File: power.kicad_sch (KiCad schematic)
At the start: 31 parts, among them Q4 CSD17575Q3, Q5 CSD17312Q5, U10 DS4432U+, U16 LM27402, U9 INA260

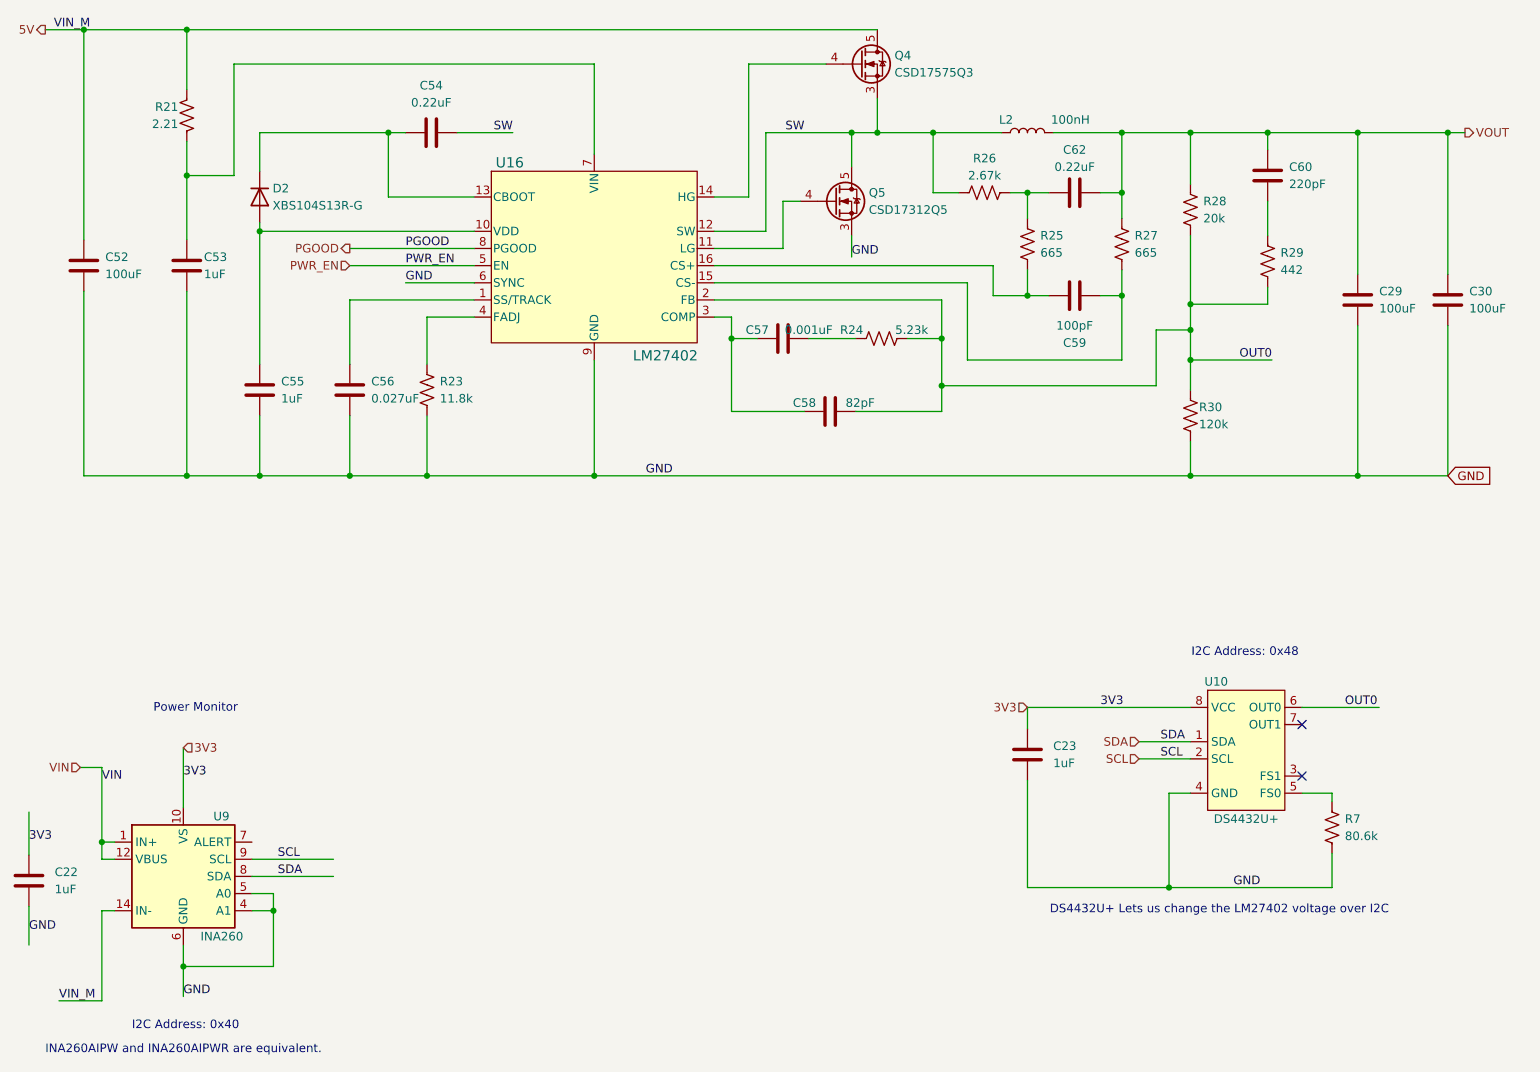
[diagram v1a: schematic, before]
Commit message: changed buttons for #5 flipped display for #2
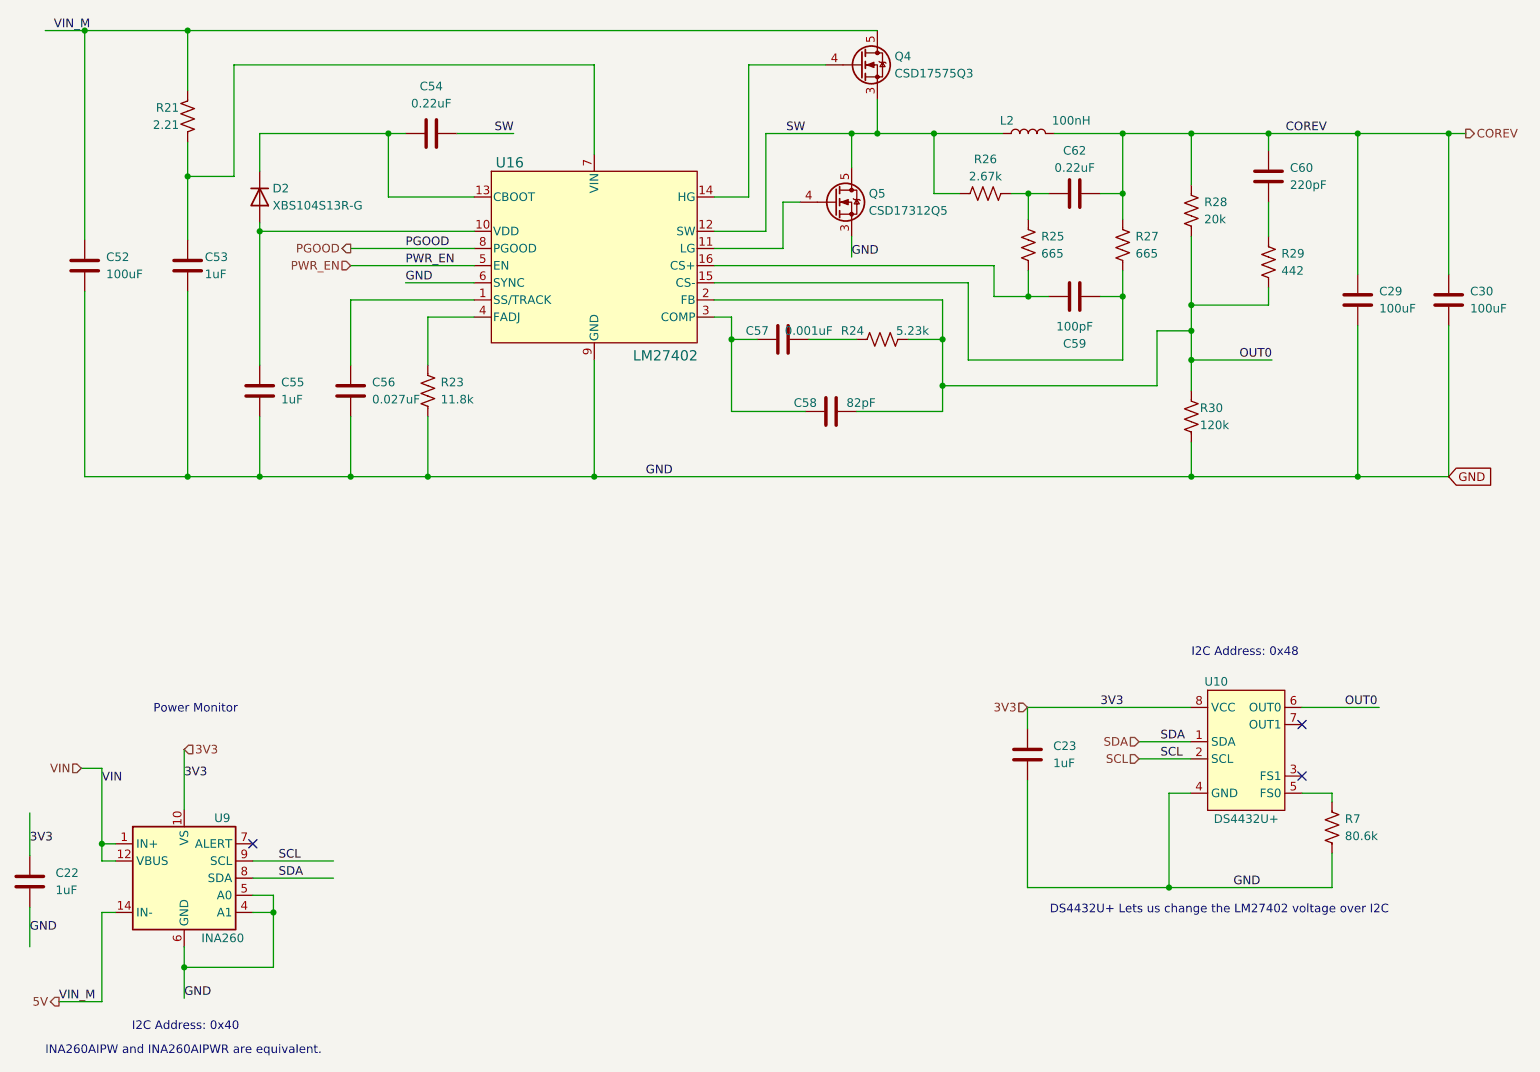
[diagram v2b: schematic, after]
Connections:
- net VIN renamed IN+
- net VOUT renamed COREV
- no-connect marks 2 -> 3

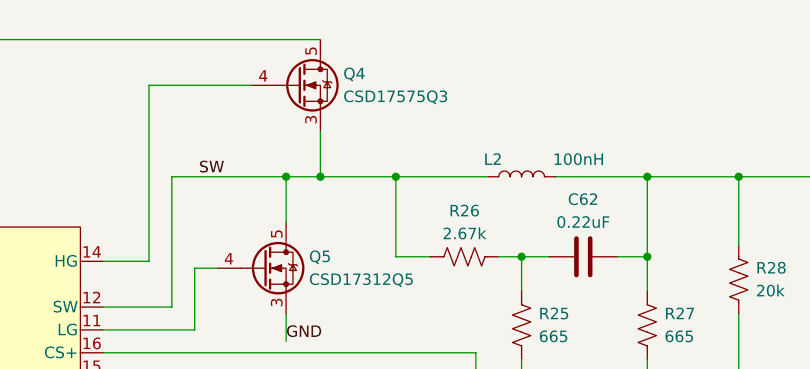
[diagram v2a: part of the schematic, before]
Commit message: switched barrel plug for #8. touched up schematic, DRC, generated BOM, generated Gerbers
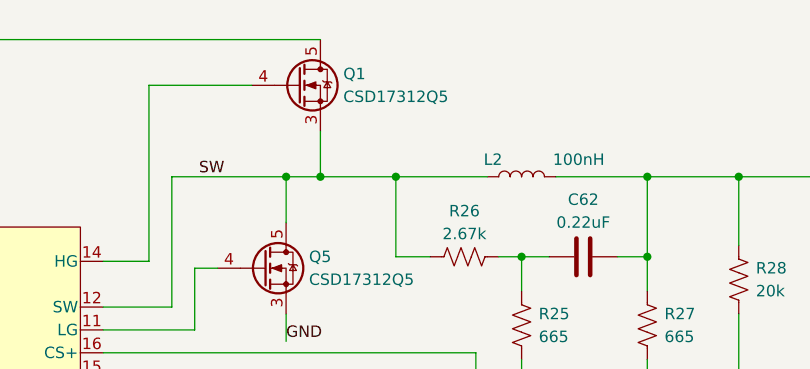
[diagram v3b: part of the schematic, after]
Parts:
- removed Q4: CSD17575Q3, blockaxe:DQG0008A, symbol blockaxe:Q_NMOS_CSD17311Q5_1
- added Q1: CSD17312Q5, blockaxe:DQH8, symbol blockaxe:Q_NMOS_CSD17311Q5_1
- R28: DK P20.0KLCT-ND -> 311-20.0KLRCT-ND; PARTNO ERJ-2RKF2002X -> RC0402FR-0720KL
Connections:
- net 5V: now also Q1.5 (D)
- net SW: now also Q1.1, Q1.2, Q1.3 (S)
- net at U16.14 (HG): now also Q1.4 (G)

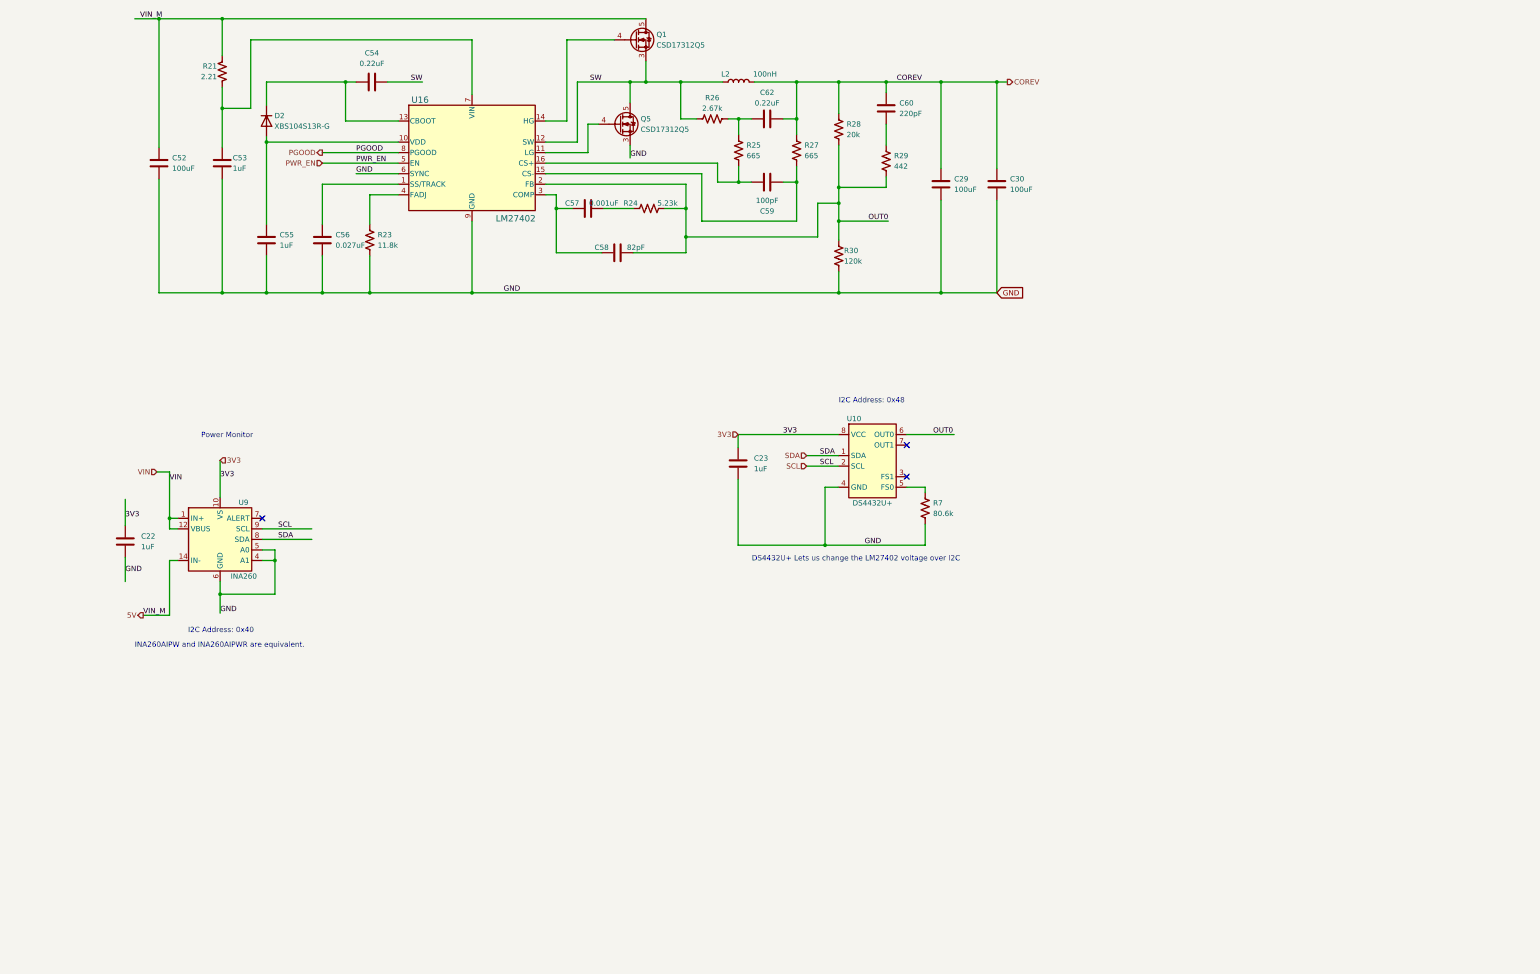
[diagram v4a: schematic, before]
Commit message: switch to bitaxeAura/GT base
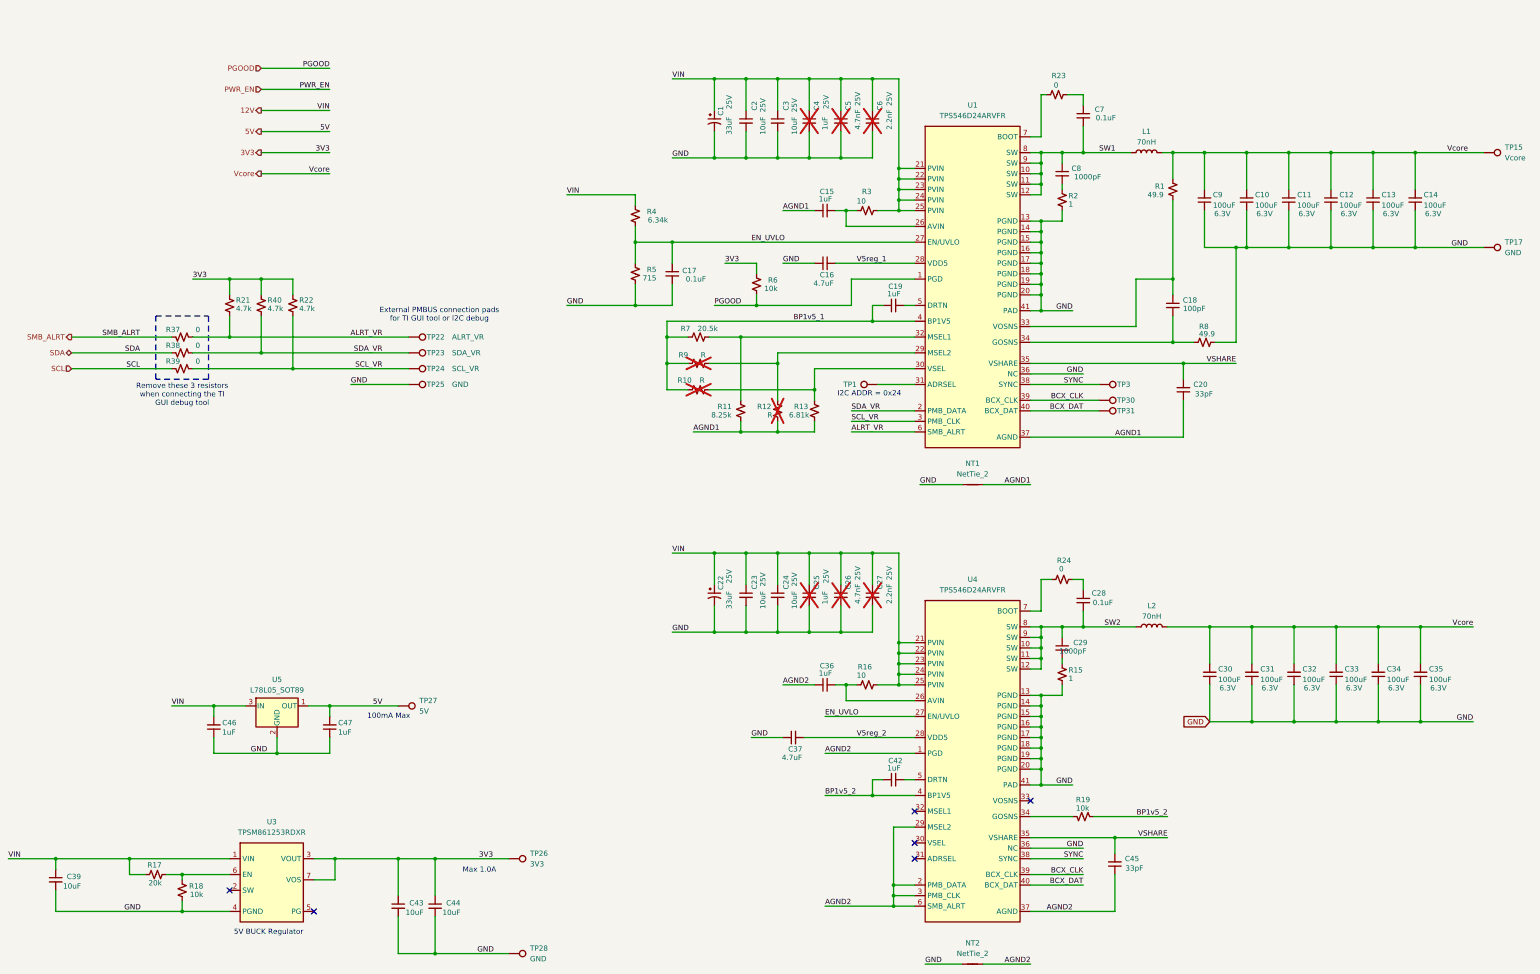
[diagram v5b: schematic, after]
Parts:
- removed C22, C23: 1uF, Capacitor_SMD:C_0402_1005Metric, symbol Device:C
- removed C29, C30, C52: 100uF, Capacitor_SMD:C_1210_3225Metric, symbol Device:C
- removed C53, C55: 1uF, Capacitor_SMD:C_0805_2012Metric, symbol Device:C
- removed C54, C62: 0.22uF, Capacitor_SMD:C_0603_1608Metric, symbol Device:C
- removed C56: 0.027uF, Capacitor_SMD:C_0402_1005Metric, symbol Device:C
- removed C57: 0.001uF, Capacitor_SMD:C_0805_2012Metric, symbol Device:C
- removed C58: 82pF, Capacitor_SMD:C_0805_2012Metric, symbol Device:C
- removed C59: 100pF, Capacitor_SMD:C_0402_1005Metric, symbol Device:C
- removed C60: 220pF, Capacitor_SMD:C_0805_2012Metric, symbol Device:C
- removed D2: XBS104S13R-G, Diode_SMD:D_SOD-323, symbol Device:D
- removed Q1, Q5: CSD17312Q5, blockaxe:DQH8, symbol blockaxe:Q_NMOS_CSD17311Q5_1
- removed R21: 2.21, Resistor_SMD:R_0402_1005Metric, symbol Device:R_US
- removed R23: 11.8k, Resistor_SMD:R_0402_1005Metric, symbol Device:R_US
- removed R24: 5.23k, Resistor_SMD:R_0402_1005Metric, symbol Device:R_US
- removed R25, R27: 665, Resistor_SMD:R_0402_1005Metric, symbol Device:R_US
- removed R26: 2.67k, Resistor_SMD:R_0402_1005Metric, symbol Device:R_US
- removed R28: 20k, Resistor_SMD:R_0402_1005Metric, symbol Device:R_US
- removed R29: 442, Resistor_SMD:R_0402_1005Metric, symbol Device:R_US
- removed R30: 120k, Resistor_SMD:R_0402_1005Metric, symbol Device:R_US
- removed R7: 80.6k, Resistor_SMD:R_0402_1005Metric, symbol Device:R_US
- removed U10: DS4432U+, Package_SO:TSSOP-8_3x3mm_P0.65mm, symbol blockaxe:DS4432U+
- removed U16: LM27402, blockaxe:SQB16A, symbol blockaxe:LM27402SQ_NOPB
- removed U9: INA260, Package_SO:TSSOP-16_4.4x5mm_P0.65mm, symbol Sensor:INA260
- added C1, C22: 33uF, Capacitor_Tantalum_SMD:CP_EIA-7343-31_Kemet-D, symbol Device:C_Polarized_Small_US
- added C10, C11, C12, C13, C14, C30, C31, C32, C33, C34, C35, C9: 100uF, Capacitor_SMD:C_1206_3216Metric, symbol Device:C_Small
- added C15, C19, C25, C36, C4, C42, C46, C47: 1uF, Capacitor_SMD:C_0402_1005Metric, symbol Device:C_Small
- added C16, C37: 4.7uF, Capacitor_SMD:C_0402_1005Metric, symbol Device:C_Small
- added C17, C28, C7: 0.1uF, Capacitor_SMD:C_0402_1005Metric, symbol Device:C_Small
- added C18: 100pF, Capacitor_SMD:C_0402_1005Metric, symbol Device:C_Small
- added C2, C23, C24, C3, C39, C43, C44: 10uF, Capacitor_SMD:C_0603_1608Metric, symbol Device:C_Small
- added C20, C45: 33pF, Capacitor_SMD:C_0402_1005Metric, symbol Device:C_Small
- added C26, C5: 4.7nF, Capacitor_SMD:C_0402_1005Metric, symbol Device:C_Small
- added C27, C6: 2.2nF, Capacitor_SMD:C_0402_1005Metric, symbol Device:C_Small
- added C29, C8: 1000pF, Capacitor_SMD:C_0805_2012Metric, symbol Device:C_Small
- added L1: 70nH, bitaxe:SLC7649, symbol Device:L
- added NT1, NT2: NetTie_2, bitaxe:NetTie-2_SMD_Pad0.2mmx1mm, symbol Device:NetTie_2
- added R1, R8: 49.9, Resistor_SMD:R_0402_1005Metric, symbol Device:R_Small_US
- added R10, R12, R9: R, Resistor_SMD:R_0402_1005Metric, symbol Device:R_Small_US
- added R11: 8.25k, Resistor_SMD:R_0402_1005Metric, symbol Device:R_Small_US
- added R13: 6.81k, Resistor_SMD:R_0402_1005Metric, symbol Device:R_Small_US
- added R15, R2: 1, Resistor_SMD:R_0805_2012Metric, symbol Device:R_Small_US
- added R16, R3: 10, Resistor_SMD:R_0402_1005Metric, symbol Device:R_Small_US
- added R17: 20k, Resistor_SMD:R_0402_1005Metric, symbol Device:R_Small_US
- added R18, R19, R6: 10k, Resistor_SMD:R_0402_1005Metric, symbol Device:R_Small_US
- added R21, R22, R40: 4.7k, Resistor_SMD:R_0402_1005Metric, symbol Device:R_Small_US
- added R23, R24, R37, R38, R39: 0, Resistor_SMD:R_0402_1005Metric, symbol Device:R_Small_US
- added R4: 6.34k, Resistor_SMD:R_0402_1005Metric, symbol Device:R_Small_US
- added R5: 715, Resistor_SMD:R_0402_1005Metric, symbol Device:R_Small_US
- added R7: 20.5k, Resistor_SMD:R_0402_1005Metric, symbol Device:R_Small_US
- added TP1: TestPoint, TestPoint:TestPoint_Pad_D1.0mm, symbol Connector:TestPoint
- added TP15: Vcore, TestPoint:TestPoint_Pad_D1.5mm, symbol Connector:TestPoint
- added TP17, TP25, TP28: GND, TestPoint:TestPoint_Pad_D1.5mm, symbol Connector:TestPoint
- added TP22: ALRT_VR, TestPoint:TestPoint_Pad_D1.5mm, symbol Connector:TestPoint
- added TP23: SDA_VR, TestPoint:TestPoint_Pad_D1.5mm, symbol Connector:TestPoint
- added TP24: SCL_VR, TestPoint:TestPoint_Pad_D1.5mm, symbol Connector:TestPoint
- added TP26: 3V3, TestPoint:TestPoint_Pad_D1.5mm, symbol Connector:TestPoint
- added TP27: 5V, TestPoint:TestPoint_Pad_D1.5mm, symbol Connector:TestPoint
- added TP3, TP30: BCX_CLK, TestPoint:TestPoint_Pad_D1.0mm, symbol Connector:TestPoint
- added TP31: BCX_DAT, TestPoint:TestPoint_Pad_D1.0mm, symbol Connector:TestPoint
- added U1, U4: TPS546D24ARVFR, bitaxe:LQFN40-CLIP, symbol bitaxe:TPS546D24
- added U3: TPSM861253RDXR, bitaxe:TPSM863257RDX, symbol bitaxe:TPSM861253RDXR
- added U5: L78L05_SOT89, Package_TO_SOT_SMD:SOT-89-3, symbol Regulator_Linear:L78L05_SOT89
- L2: value 100nH -> 70nH; footprint blockaxe:FP0805R1-R10-R -> bitaxe:SLC7649; DK 283-FP0805R1-R10-RCT-ND -> 2457-SLC7649S-700KLD-ND; PARTNO FP0805R1-R10-R -> SLC7649S-700KLB
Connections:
- net 3V3: now also C43.1, C44.1, R21.1, R22.1, R40.1, R6.2, TP26.1, U3.3 (VOUT), U3.7 (VOS)
- net 5V: now also C47.2, TP27.1, U5.1 (OUT)
- net PGOOD: now also R6.1, U1.1 (PGD)
- net SCL: now also R39.1
- net SDA: now also R38.1
- net COREV renamed Vcore
- net Vcore: now also C10.2, C11.2, C12.2, C13.2, C14.2, C30.2, C31.2, C32.2, C33.2, C34.2, C35.2, C9.2, L1.2, R1.1, TP15.1
- net SW renamed SW2
- net SW2: now also C28.2, C29.1, U4.10 (SW), U4.11 (SW), U4.12 (SW), U4.8 (SW), U4.9 (SW)
- new net: C18.2, R8.1, U1.34 (GOSNS)
- new net: R12.2, R9.1, U1.29 (MSEL2)
- new net: R11.1, R7.1, U1.32 (MSEL1)
- new net: R17.1, R18.2, U3.6 (EN)
- new net: C19.2, U1.5 (DRTN)
- new net: C18.1, R1.2, U1.33 (VOSNS)
- new net: C29.2, R15.1
- new net: C15.2, R3.2, U1.26 (AVIN)
- new net: C28.1, R24.1
- new net: TP1.1, U1.31 (ADRSEL)
- new net: R10.1, R13.2, U1.30 (VSEL)
- new net: R23.2, U1.7 (BOOT)
- new net: R19.2, U4.34 (GOSNS)
- new net: C7.1, R23.1
- new net: C8.2, R2.1
- new net: C36.2, R16.2, U4.26 (AVIN)
- new net: C42.2, U4.5 (DRTN)
- new net: R24.2, U4.7 (BOOT)
- new net 12V: C1.1, C2.1, C22.1, C23.1, C24.1, C25.1, C26.1, C27.1, C3.1, C39.1, C4.1, C46.2, C5.1, C6.1, R16.1, R17.2, R3.1, R4.2, U1.21 (PVIN), U1.22 (PVIN), U1.23 (PVIN), U1.24 (PVIN), U1.25 (PVIN), U3.1 (VIN), U4.21 (PVIN), U4.22 (PVIN), U4.23 (PVIN), U4.24 (PVIN), U4.25 (PVIN), U5.3 (IN)
- new net AGND1: C15.1, C20.1, NT1.2, R11.2, R12.1, R13.1, U1.37 (AGND)
- new net AGND2: C36.1, C45.1, NT2.2, U4.1 (PGD), U4.2 (PMB_DATA), U4.29 (MSEL2), U4.3 (PMB_CLK), U4.37 (AGND), U4.6 (SMB_ALRT)
- new net ALRT_VR: R21.2, R37.2, TP22.1, U1.6 (SMB_ALRT)
- new net BCX_CLK: TP30.1, U1.39 (BCX_CLK), U4.39 (BCX_CLK)
- new net BCX_DAT: TP31.1, U1.40 (BCX_DAT), U4.40 (BCX_DAT)
- new net BP1v5_1: C19.1, R10.2, R7.2, R9.2, U1.4 (BP1V5)
- new net BP1v5_2: C42.1, R19.1, U4.4 (BP1V5)
- new net EN_UVLO: C17.1, R4.1, R5.2, U1.27 (EN/UVLO), U4.27 (EN/UVLO)
- new net GND: C1.2, C10.1, C11.1, C12.1, C13.1, C14.1, C16.1, C17.2, C2.2, C22.2, C23.2, C24.2, C25.2, C26.2, C27.2, C3.2, C30.1, C31.1, C32.1, C33.1, C34.1, C35.1, C37.1, C39.2, C4.2, C43.2, C44.2, C46.1, C47.1, C5.2, C6.2, C9.1, NT1.1, NT2.1, R15.2, R18.1, R2.2, R5.1, R8.2, TP17.1, TP25.1, TP28.1, U1.13 (PGND), U1.14 (PGND), U1.15 (PGND), U1.16 (PGND), U1.17 (PGND), U1.18 (PGND), U1.19 (PGND), U1.20 (PGND), U1.36 (NC), U1.41 (PAD), U3.4 (PGND), U4.13 (PGND), U4.14 (PGND), U4.15 (PGND), U4.16 (PGND), U4.17 (PGND), U4.18 (PGND), U4.19 (PGND), U4.20 (PGND), U4.36 (NC), U4.41 (PAD), U5.2 (GND)
- new net SCL_VR: R22.2, R39.2, TP24.1, U1.3 (PMB_CLK)
- new net SDA_VR: R38.2, R40.2, TP23.1, U1.2 (PMB_DATA)
- new net SMB_ALRT: R37.1
- new net SW1: C7.2, C8.1, L1.1, U1.10 (SW), U1.11 (SW), U1.12 (SW), U1.8 (SW), U1.9 (SW)
- new net SYNC: TP3.1, U1.38 (SYNC), U4.38 (SYNC)
- new net V5reg_1: C16.2, U1.28 (VDD5)
- new net V5reg_2: C37.2, U4.28 (VDD5)
- new net VSHARE: C20.2, C45.2, U1.35 (VSHARE), U4.35 (VSHARE)
- no-connect marks 3 -> 6
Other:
- note added: "100mA Max"
- note added: "5V BUCK Regulator"
- note added: "External PMBUS connection pads for TI GUI tool or I2C debug"
- note added: "I2C ADDR = 0x24"
- note added: "Max 1.0A"
- note added: "Remove these 3 resistors when connecting the TI GUI debug tool"
- note removed: "DS4432U+ Lets us change the LM27402 voltage over I2C"
- note removed: "I2C Address: 0x40"
- note removed: "I2C Address: 0x48"
- note removed: "INA260AIPW and INA260AIPWR are equivalent."
- note removed: "Power Monitor"
- title: blockaxe1 -> bitaxeBonanza
